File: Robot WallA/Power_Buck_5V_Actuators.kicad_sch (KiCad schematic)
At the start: 16 parts, among them J16 NID35-5, Q4 BSS138

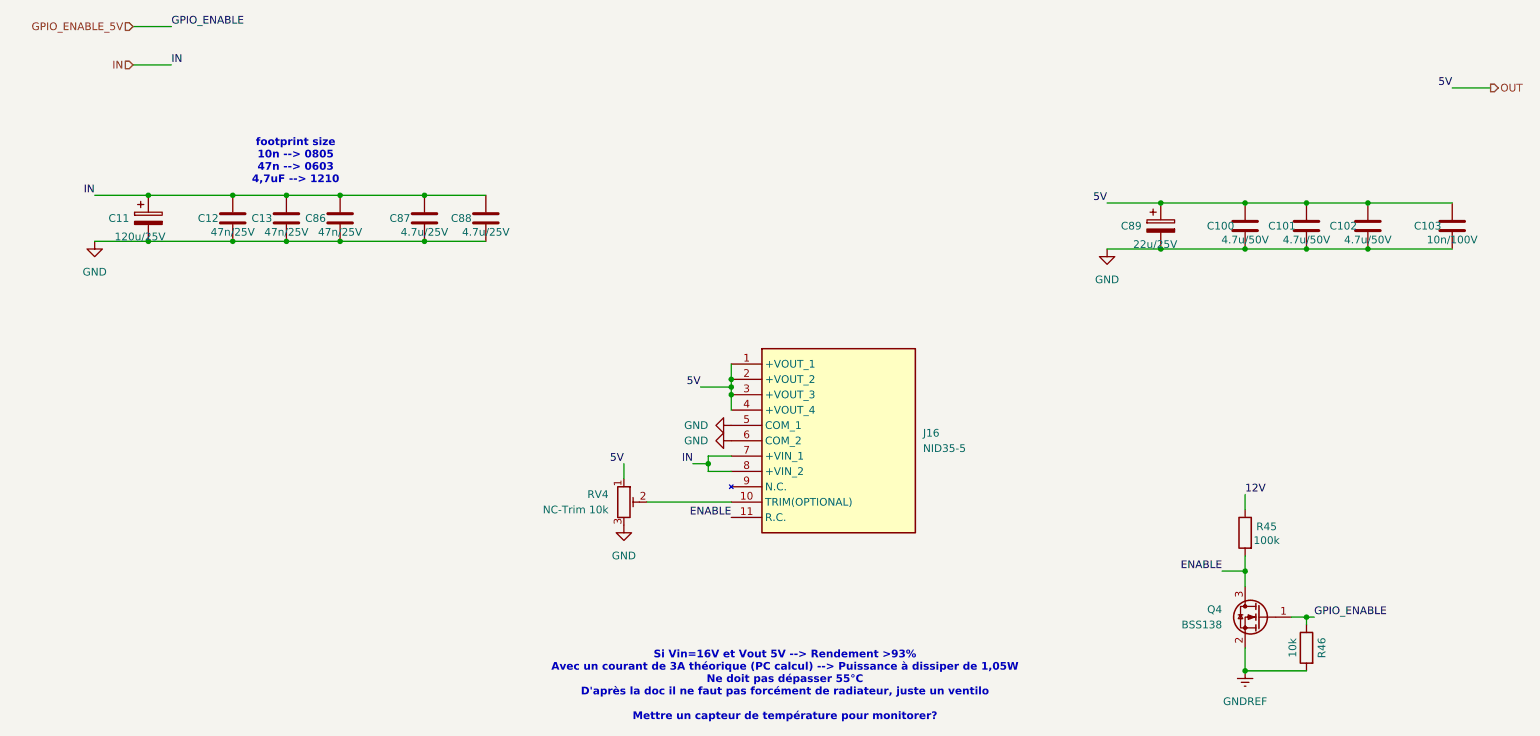
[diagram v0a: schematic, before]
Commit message: Continued to link MCU pins, Added a sheet for servomotors and optional 2 DC motors.
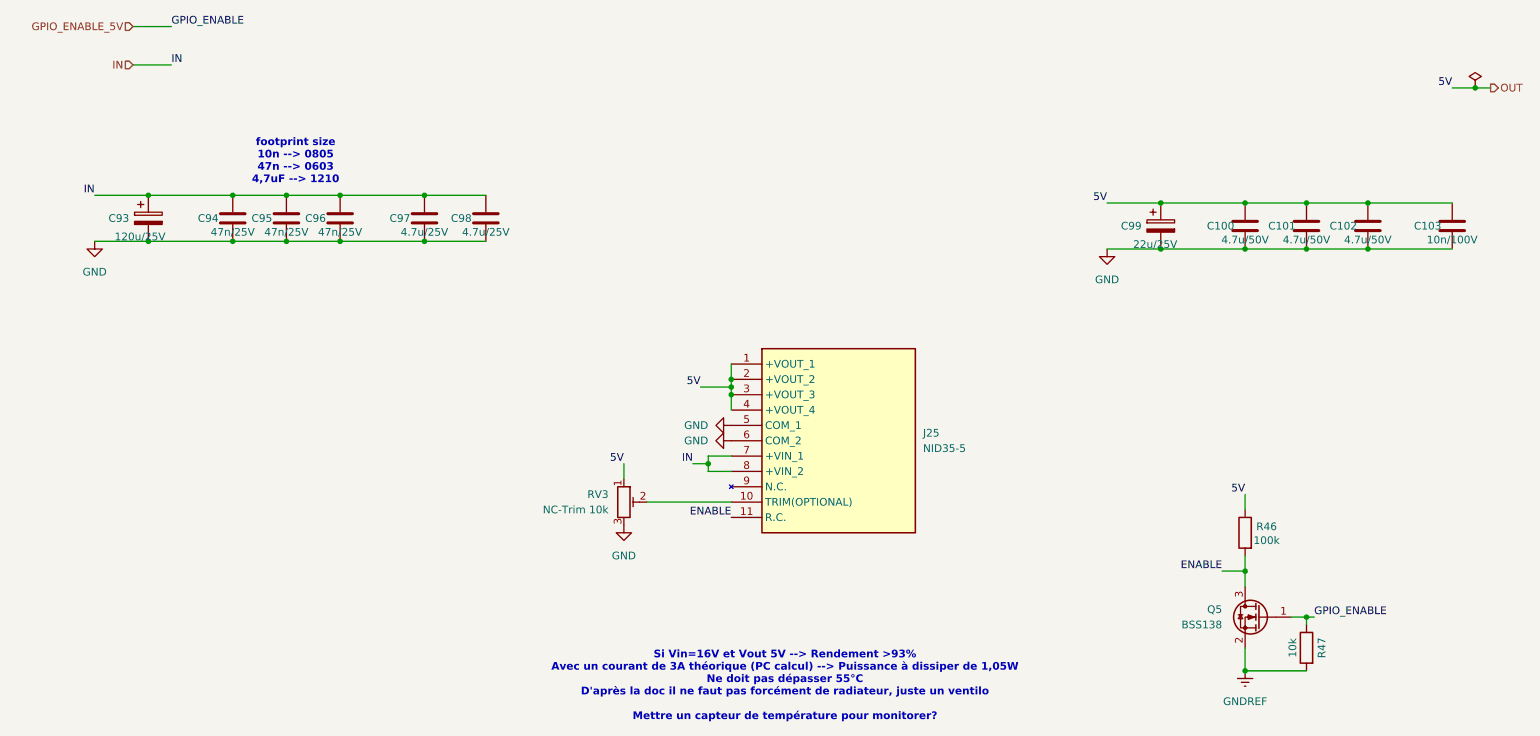
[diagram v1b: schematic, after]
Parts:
- renumbered C11 to C93, C12 to C94, C13 to C95, C86 to C96, C87 to C97, C88 to C98, C89 to C99, J16 to J25, Q4 to Q5, R45 to R46, R46 to R47, RV4 to RV3
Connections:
- net 12V is gone; now on net OUT: R46.1
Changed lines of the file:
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@@
+	)
+	(junction
+		(at 261.62 29.21)
+		(diameter 0)
+		(color 0 0 0 0)
 	)
 	(junction
@@
 	(wire
 		(pts
-			(xy 257.81 29.21) (xy 264.16 29.21)
+			(xy 257.81 29.21) (xy 261.62 29.21)
 		)
 		(stroke
@@
 		(pts
 			(xy 134.62 91.44) (xy 134.62 90.17)
+		)
+		(stroke
+			(width 0)
+			(type default)
+		)
+	)
+	(wire
+		(pts
+			(xy 261.62 29.21) (xy 264.16 29.21)
 		)
 		(stroke
@@
 	)
 	(label "5V"
+		(at 223.52 96.52 180)
+		(effects
+			(font
+				(size 1.27 1.27)
+			)
+			(justify right bottom)
+		)
+	)
+	(label "5V"
 		(at 120.65 91.44 180)
 		(effects
@@
 	(label "GPIO_ENABLE"
 		(at 45.72 19.05 0)
-		(effects
-			(font
-				(size 1.27 1.27)
-			)
-			(justify left bottom)
-		)
-	)
-	(label "12V"
-		(at 223.52 96.52 0)
 		(effects
 			(font
@@
 		(dnp no)
 		(fields_autoplaced yes)
-		(property "Reference" "RV4"
+		(property "Reference" "RV3"
 			(at 118.11 96.5199 0)
 			(effects
@@
 			(project "PCB"
 				(path "/117fd49e-499d-4b54-b58c-f6b538ecca4a/d5f4dab0-e2de-4083-971d-4b1eb9c8d4bb/1e067d8d-e8a8-481d-ab40-c8016ce22eb0"
-					(reference "RV4")
+					(reference "RV3")
 					(unit 1)
 				)
@@
 		(dnp no)
 		(fields_autoplaced yes)
-		(property "Reference" "#PWR039"
+		(property "Reference" "#PWR0105"
 			(at 33.02 60.96 0)
 			(effects
@@
 			(project "PCB"
 				(path "/117fd49e-499d-4b54-b58c-f6b538ecca4a/d5f4dab0-e2de-4083-971d-4b1eb9c8d4bb/1e067d8d-e8a8-481d-ab40-c8016ce22eb0"
-					(reference "#PWR039")
+					(reference "#PWR0105")
 					(unit 1)
 				)
@@
 		(on_board yes)
 		(dnp no)
-		(property "Reference" "C11"
+		(property "Reference" "C93"
 			(at 35.306 50.8 0)
 			(effects
@@
 			(project "PCB"
 				(path "/117fd49e-499d-4b54-b58c-f6b538ecca4a/d5f4dab0-e2de-4083-971d-4b1eb9c8d4bb/1e067d8d-e8a8-481d-ab40-c8016ce22eb0"
-					(reference "C11")
+					(reference "C93")
 					(unit 1)
 				)
@@
 		(dnp no)
 		(fields_autoplaced yes)
-		(property "Reference" "J16"
+		(property "Reference" "J25"
 			(at 170.18 86.3599 0)
 			(effects
@@
 			(project "PCB"
 				(path "/117fd49e-499d-4b54-b58c-f6b538ecca4a/d5f4dab0-e2de-4083-971d-4b1eb9c8d4bb/1e067d8d-e8a8-481d-ab40-c8016ce22eb0"
-					(reference "J16")
+					(reference "J25")
 					(unit 1)
 				)
@@
 		(on_board yes)
 		(dnp no)
-		(property "Reference" "C86"
+		(property "Reference" "C96"
 			(at 69.596 50.8 0)
 			(effects
@@
 			(project "PCB"
 				(path "/117fd49e-499d-4b54-b58c-f6b538ecca4a/d5f4dab0-e2de-4083-971d-4b1eb9c8d4bb/1e067d8d-e8a8-481d-ab40-c8016ce22eb0"
-					(reference "C86")
+					(reference "C96")
 					(unit 1)
 				)
@@
 		(dnp no)
 		(fields_autoplaced yes)
-		(property "Reference" "#PWR0102"
+		(property "Reference" "#PWR0108"
 			(at 132.08 87.63 0)
 			(effects
@@
 			(project "PCB"
 				(path "/117fd49e-499d-4b54-b58c-f6b538ecca4a/d5f4dab0-e2de-4083-971d-4b1eb9c8d4bb/1e067d8d-e8a8-481d-ab40-c8016ce22eb0"
-					(reference "#PWR0102")
+					(reference "#PWR0108")
 					(unit 1)
 				)
@@
 		(on_board yes)
 		(dnp no)
-		(property "Reference" "R45"
+		(property "Reference" "R46"
 			(at 227.076 101.854 0)
 			(effects
@@
 			(project "PCB"
 				(path "/117fd49e-499d-4b54-b58c-f6b538ecca4a/d5f4dab0-e2de-4083-971d-4b1eb9c8d4bb/1e067d8d-e8a8-481d-ab40-c8016ce22eb0"
-					(reference "R45")
+					(reference "R46")
+					(unit 1)
+				)
+			)
+		)
+	)
+	(symbol
+		(lib_id "power:PWR_FLAG")
+		(at 261.62 29.21 0)
+		(unit 1)
+		(exclude_from_sim no)
+		(in_bom yes)
+		(on_board yes)
+		(dnp no)
+		(fields_autoplaced yes)
+		(property "Reference" "#FLG06"
+			(at 261.62 27.305 0)
+			(effects
+				(font
+					(size 1.27 1.27)
+				)
+				(hide yes)
+			)
+		)
+		(property "Value" "PWR_FLAG"
+			(at 261.62 24.13 0)
+			(effects
+				(font
+					(size 1.27 1.27)
+				)
+				(hide yes)
+			)
+		)
+		(property "Footprint" ""
+			(at 261.62 29.21 0)
+			(effects
+				(font
+					(size 1.27 1.27)
+				)
+				(hide yes)
+			)
+		)
+		(property "Datasheet" "~"
+			(at 261.62 29.21 0)
+			(effects
+				(font
+					(size 1.27 1.27)
+				)
+				(hide yes)
+			)
+		)
+		(property "Description" "Special symbol for telling ERC where power comes from"
+			(at 261.62 29.21 0)
+			(effects
+				(font
+					(size 1.27 1.27)
+				)
+				(hide yes)
+			)
+		)
+		(pin "1"
+		)
+		(instances
+			(project "Robot WallA"
+				(path "/117fd49e-499d-4b54-b58c-f6b538ecca4a/d5f4dab0-e2de-4083-971d-4b1eb9c8d4bb/1e067d8d-e8a8-481d-ab40-c8016ce22eb0"
+					(reference "#FLG06")
 					(unit 1)
 				)
@@
 		(on_board yes)
 		(dnp no)
-		(property "Reference" "C89"
+		(property "Reference" "C99"
 			(at 202.946 52.07 0)
 			(effects
@@
 			(project "PCB"
 				(path "/117fd49e-499d-4b54-b58c-f6b538ecca4a/d5f4dab0-e2de-4083-971d-4b1eb9c8d4bb/1e067d8d-e8a8-481d-ab40-c8016ce22eb0"
-					(reference "C89")
+					(reference "C99")
 					(unit 1)
 				)
@@
 		(dnp no)
 		(fields_autoplaced yes)
-		(property "Reference" "#PWR023"
+		(property "Reference" "#PWR0110"
 			(at 223.52 132.08 0)
 			(effects
@@
 			(project "PCB"
 				(path "/117fd49e-499d-4b54-b58c-f6b538ecca4a/d5f4dab0-e2de-4083-971d-4b1eb9c8d4bb/1e067d8d-e8a8-481d-ab40-c8016ce22eb0"
-					(reference "#PWR023")
+					(reference "#PWR0110")
 					(unit 1)
 				)
@@
 		(dnp no)
 		(fields_autoplaced yes)
-		(property "Reference" "#PWR040"
+		(property "Reference" "#PWR0106"
 			(at 120.65 107.95 0)
 			(effects
@@
 			(project "PCB"
 				(path "/117fd49e-499d-4b54-b58c-f6b538ecca4a/d5f4dab0-e2de-4083-971d-4b1eb9c8d4bb/1e067d8d-e8a8-481d-ab40-c8016ce22eb0"
-					(reference "#PWR040")
+					(reference "#PWR0106")
 					(unit 1)
 				)
@@
 		(on_board yes)
 		(dnp no)
-		(property "Reference" "C13"
+		(property "Reference" "C95"
 			(at 60.706 50.8 0)
 			(effects
@@
 			(project "PCB"
 				(path "/117fd49e-499d-4b54-b58c-f6b538ecca4a/d5f4dab0-e2de-4083-971d-4b1eb9c8d4bb/1e067d8d-e8a8-481d-ab40-c8016ce22eb0"
-					(reference "C13")
+					(reference "C95")
 					(unit 1)
 				)
@@
 		(on_board yes)
 		(dnp no)
-		(property "Reference" "C87"
+		(property "Reference" "C97"
 			(at 83.566 50.8 0)
 			(effects
@@
 			(project "PCB"
 				(path "/117fd49e-499d-4b54-b58c-f6b538ecca4a/d5f4dab0-e2de-4083-971d-4b1eb9c8d4bb/1e067d8d-e8a8-481d-ab40-c8016ce22eb0"
-					(reference "C87")
+					(reference "C97")
 					(unit 1)
 				)
@@
 		(dnp no)
 		(fields_autoplaced yes)
-		(property "Reference" "Q4"
+		(property "Reference" "Q5"
 			(at 219.71 115.5699 0)
 			(effects
@@
 			(project "PCB"
 				(path "/117fd49e-499d-4b54-b58c-f6b538ecca4a/d5f4dab0-e2de-4083-971d-4b1eb9c8d4bb/1e067d8d-e8a8-481d-ab40-c8016ce22eb0"
-					(reference "Q4")
+					(reference "Q5")
 					(unit 1)
 				)
@@
 		(dnp no)
 		(fields_autoplaced yes)
-		(property "Reference" "#PWR0103"
+		(property "Reference" "#PWR0109"
 			(at 200.66 62.23 0)
 			(effects
@@
 			(project "PCB"
 				(path "/117fd49e-499d-4b54-b58c-f6b538ecca4a/d5f4dab0-e2de-4083-971d-4b1eb9c8d4bb/1e067d8d-e8a8-481d-ab40-c8016ce22eb0"
-					(reference "#PWR0103")
+					(reference "#PWR0109")
 					(unit 1)
 				)
@@
 		(dnp no)
 		(fields_autoplaced yes)
-		(property "Reference" "#PWR041"
+		(property "Reference" "#PWR0107"
 			(at 132.08 85.09 0)
 			(effects
@@
 			(project "PCB"
 				(path "/117fd49e-499d-4b54-b58c-f6b538ecca4a/d5f4dab0-e2de-4083-971d-4b1eb9c8d4bb/1e067d8d-e8a8-481d-ab40-c8016ce22eb0"
-					(reference "#PWR041")
+					(reference "#PWR0107")
 					(unit 1)
 				)
@@
 		(on_board yes)
 		(dnp no)
-		(property "Reference" "C12"
+		(property "Reference" "C94"
 			(at 51.816 50.8 0)
 			(effects
@@
 			(project "PCB"
 				(path "/117fd49e-499d-4b54-b58c-f6b538ecca4a/d5f4dab0-e2de-4083-971d-4b1eb9c8d4bb/1e067d8d-e8a8-481d-ab40-c8016ce22eb0"
-					(reference "C12")
+					(reference "C94")
 					(unit 1)
 				)
@@
 		(on_board yes)
 		(dnp no)
-		(property "Reference" "R46"
+		(property "Reference" "R47"
 			(at 236.22 121.92 90)
 			(effects
@@
 			(project "PCB"
 				(path "/117fd49e-499d-4b54-b58c-f6b538ecca4a/d5f4dab0-e2de-4083-971d-4b1eb9c8d4bb/1e067d8d-e8a8-481d-ab40-c8016ce22eb0"
-					(reference "R46")
+					(reference "R47")
 					(unit 1)
 				)
@@
 		(on_board yes)
 		(dnp no)
-		(property "Reference" "C88"
+		(property "Reference" "C98"
 			(at 93.726 50.8 0)
 			(effects
@@
 			(project "PCB"
 				(path "/117fd49e-499d-4b54-b58c-f6b538ecca4a/d5f4dab0-e2de-4083-971d-4b1eb9c8d4bb/1e067d8d-e8a8-481d-ab40-c8016ce22eb0"
-					(reference "C88")
-					(unit 1)
-				)
+					(reference "C98")
+					(unit 1)
+				)

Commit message: Defined every footprints
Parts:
- added D16: LED_RED, LED_SMD:LED_0603_1608Metric, symbol Device:LED
- added R53: 1.6k, Resistor_SMD:R_0603_1608Metric_Pad0.98x0.95mm_HandSolder, symbol Device:R
- C51: renamed from C93; value 120u/25V -> 120uF/25V; footprint (none) -> SamacSys_Parts:EEE0JA331XP; Manufacturer_Part_Number (none) -> EEE-FNV121XUP
- C52: renamed from C94; value 47n/25V -> 47nF/25V; footprint (none) -> Capacitor_SMD:C_0603_1608Metric_Pad1.08x0.95mm_HandSolder
- C53: renamed from C95; value 47n/25V -> 47nF/25V; footprint (none) -> Capacitor_SMD:C_0603_1608Metric_Pad1.08x0.95mm_HandSolder
- C54: renamed from C96; value 47n/25V -> 47nF/25V; footprint (none) -> Capacitor_SMD:C_0603_1608Metric_Pad1.08x0.95mm_HandSolder
- C55: renamed from C97; value 4.7u/25V -> 4.7uF/25V; footprint (none) -> Capacitor_SMD:C_1210_3225Metric_Pad1.33x2.70mm_HandSolder
- C56: renamed from C98; value 4.7u/25V -> 4.7uF/25V; footprint (none) -> Capacitor_SMD:C_1210_3225Metric_Pad1.33x2.70mm_HandSolder
- C57: renamed from C99; value 22u/25V -> 22uF/25V; footprint (none) -> Capacitor_SMD:C_0805_2012Metric_Pad1.18x1.45mm_HandSolder
- C58: renamed from C100; value 4.7u/50V -> 4.7uF/50V; footprint (none) -> Capacitor_SMD:C_0805_2012Metric_Pad1.18x1.45mm_HandSolder
- C59: renamed from C101; value 4.7u/50V -> 4.7uF/50V; footprint (none) -> Capacitor_SMD:C_0805_2012Metric_Pad1.18x1.45mm_HandSolder
- C60: renamed from C102; value 4.7u/50V -> 4.7uF/50V; footprint (none) -> Capacitor_SMD:C_0805_2012Metric_Pad1.18x1.45mm_HandSolder
- C61: renamed from C103; value 10n/100V -> 10nF/50V; footprint (none) -> Capacitor_SMD:C_0805_2012Metric_Pad1.18x1.45mm_HandSolder
- J12: renamed from J25; footprint NID355 -> SamacSys_Parts:NID355; Arrow Part Number NID35-5 -> (none); Arrow Price/Stock https://www.arrow.com/en/products/nid35-5/mean-well-enterpr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 -> (none); Height 13 -> (none); Manufacturer_Name Mean Well -> (none); Mouser Part Number 709-NID35-5 -> (none); Mouser Price/Stock https://www.mouser.co.uk/ProductDetail/MEAN-WELL/NID35-5?qs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 -> (none)
- R30: renamed from R46; footprint (none) -> Resistor_SMD:R_0603_1608Metric_Pad0.98x0.95mm_HandSolder
- R31: renamed from R47; footprint (none) -> Resistor_SMD:R_0603_1608Metric_Pad0.98x0.95mm_HandSolder
- RV2: renamed from RV3; value NC-Trim 10k -> Trim 10k; footprint (none) -> SamacSys_Parts:TC33X2503E; now not fitted
- renumbered Q5 to Q1
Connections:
- net GND: now also R53.2
- net OUT: now also D16.2 (A)
- new net: D16.1 (K), R53.1

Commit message: Updated USB UART converter, Linked telemeter sensors.
Updated components indicators
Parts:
- Q1: Manufacturer_Part_Number (none) -> BSS138
- RV2: Manufacturer_Part_Number (none) -> TC33X2503E
- renumbered D16 to D5, J12 to J14, R53 to R30, R30 to R31, R31 to R32
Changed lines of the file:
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@@
+			)
+		)
+		(property "Manufacturer_Part_Number" "TC33X2503E"
+			(at 120.65 97.79 0)
+			(effects
+				(font
+					(size 1.27 1.27)
+				)
+				(hide yes)
 			)
 		)
@@
 		(dnp no)
 		(fields_autoplaced yes)
-		(property "Reference" "#PWR059"
+		(property "Reference" "#PWR062"
 			(at 33.02 60.96 0)
 			(effects
@@
 			(project "PCB"
 				(path "/117fd49e-499d-4b54-b58c-f6b538ecca4a/d5f4dab0-e2de-4083-971d-4b1eb9c8d4bb/1e067d8d-e8a8-481d-ab40-c8016ce22eb0"
-					(reference "#PWR059")
+					(reference "#PWR062")
 					(unit 1)
 				)
@@
 		(dnp no)
 		(fields_autoplaced yes)
-		(property "Reference" "J12"
+		(property "Reference" "J14"
 			(at 170.18 86.3599 0)
 			(effects
@@
 			(project "PCB"
 				(path "/117fd49e-499d-4b54-b58c-f6b538ecca4a/d5f4dab0-e2de-4083-971d-4b1eb9c8d4bb/1e067d8d-e8a8-481d-ab40-c8016ce22eb0"
-					(reference "J12")
+					(reference "J14")
 					(unit 1)
 				)
@@
 		(dnp no)
 		(fields_autoplaced yes)
-		(property "Reference" "#PWR062"
+		(property "Reference" "#PWR065"
 			(at 132.08 87.63 0)
 			(effects
@@
 			(project "PCB"
 				(path "/117fd49e-499d-4b54-b58c-f6b538ecca4a/d5f4dab0-e2de-4083-971d-4b1eb9c8d4bb/1e067d8d-e8a8-481d-ab40-c8016ce22eb0"
-					(reference "#PWR062")
+					(reference "#PWR065")
 					(unit 1)
 				)
@@
 		(on_board yes)
 		(dnp no)
-		(property "Reference" "R30"
+		(property "Reference" "R31"
 			(at 227.076 101.854 0)
 			(effects
@@
 			(project "PCB"
 				(path "/117fd49e-499d-4b54-b58c-f6b538ecca4a/d5f4dab0-e2de-4083-971d-4b1eb9c8d4bb/1e067d8d-e8a8-481d-ab40-c8016ce22eb0"
-					(reference "R30")
+					(reference "R31")
 					(unit 1)
 				)
@@
 		(on_board yes)
 		(dnp no)
-		(property "Reference" "R53"
+		(property "Reference" "R30"
 			(at 154.94 49.53 90)
 			(effects
@@
 			(project "Robot WallA"
 				(path "/117fd49e-499d-4b54-b58c-f6b538ecca4a/d5f4dab0-e2de-4083-971d-4b1eb9c8d4bb/1e067d8d-e8a8-481d-ab40-c8016ce22eb0"
-					(reference "R53")
+					(reference "R30")
 					(unit 1)
 				)
@@
 		(dnp no)
 		(fields_autoplaced yes)
-		(property "Reference" "#PWR0126"
+		(property "Reference" "#PWR061"
 			(at 165.1 49.53 0)
 			(effects
@@
 			(project "Robot WallA"
 				(path "/117fd49e-499d-4b54-b58c-f6b538ecca4a/d5f4dab0-e2de-4083-971d-4b1eb9c8d4bb/1e067d8d-e8a8-481d-ab40-c8016ce22eb0"
-					(reference "#PWR0126")
+					(reference "#PWR061")
 					(unit 1)
 				)
@@
 		(dnp no)
 		(fields_autoplaced yes)
-		(property "Reference" "#PWR064"
+		(property "Reference" "#PWR067"
 			(at 223.52 132.08 0)
 			(effects
@@
 			(project "PCB"
 				(path "/117fd49e-499d-4b54-b58c-f6b538ecca4a/d5f4dab0-e2de-4083-971d-4b1eb9c8d4bb/1e067d8d-e8a8-481d-ab40-c8016ce22eb0"
-					(reference "#PWR064")
+					(reference "#PWR067")
 					(unit 1)
 				)
@@
 		(dnp no)
 		(fields_autoplaced yes)
-		(property "Reference" "#PWR063"
+		(property "Reference" "#PWR066"
 			(at 120.65 107.95 0)
 			(effects
@@
 			(project "PCB"
 				(path "/117fd49e-499d-4b54-b58c-f6b538ecca4a/d5f4dab0-e2de-4083-971d-4b1eb9c8d4bb/1e067d8d-e8a8-481d-ab40-c8016ce22eb0"
-					(reference "#PWR063")
+					(reference "#PWR066")
 					(unit 1)
 				)
@@
 		)
 		(property "Description" "50V Vds, 0.22A Id, N-Channel MOSFET, SOT-23"
+			(at 226.06 116.84 0)
+			(effects
+				(font
+					(size 1.27 1.27)
+				)
+				(hide yes)
+			)
+		)
+		(property "Manufacturer_Part_Number" "BSS138"
 			(at 226.06 116.84 0)
 			(effects
@@
 		(on_board yes)
 		(dnp no)
-		(property "Reference" "D16"
+		(property "Reference" "D5"
 			(at 144.78 46.99 0)
 			(effects
@@
 			(project "Robot WallA"
 				(path "/117fd49e-499d-4b54-b58c-f6b538ecca4a/d5f4dab0-e2de-4083-971d-4b1eb9c8d4bb/1e067d8d-e8a8-481d-ab40-c8016ce22eb0"
-					(reference "D16")
+					(reference "D5")
 					(unit 1)
 				)
@@
 		(dnp no)
 		(fields_autoplaced yes)
-		(property "Reference" "#PWR060"
+		(property "Reference" "#PWR063"
 			(at 200.66 62.23 0)
 			(effects
@@
 			(project "PCB"
 				(path "/117fd49e-499d-4b54-b58c-f6b538ecca4a/d5f4dab0-e2de-4083-971d-4b1eb9c8d4bb/1e067d8d-e8a8-481d-ab40-c8016ce22eb0"
-					(reference "#PWR060")
+					(reference "#PWR063")
 					(unit 1)
 				)
@@
 		(dnp no)
 		(fields_autoplaced yes)
-		(property "Reference" "#PWR061"
+		(property "Reference" "#PWR064"
 			(at 132.08 85.09 0)
 			(effects
@@
 			(project "PCB"
 				(path "/117fd49e-499d-4b54-b58c-f6b538ecca4a/d5f4dab0-e2de-4083-971d-4b1eb9c8d4bb/1e067d8d-e8a8-481d-ab40-c8016ce22eb0"
-					(reference "#PWR061")
+					(reference "#PWR064")
 					(unit 1)
 				)
@@
 		(on_board yes)
 		(dnp no)
-		(property "Reference" "R31"
+		(property "Reference" "R32"
 			(at 236.22 121.92 90)
 			(effects
@@
 			(project "PCB"
 				(path "/117fd49e-499d-4b54-b58c-f6b538ecca4a/d5f4dab0-e2de-4083-971d-4b1eb9c8d4bb/1e067d8d-e8a8-481d-ab40-c8016ce22eb0"
-					(reference "R31")
-					(unit 1)
-				)
+					(reference "R32")
+					(unit 1)
+				)
